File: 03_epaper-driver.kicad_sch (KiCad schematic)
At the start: 28 parts, among them J7 FFC2B28-24-G, Q1 Si1308EDL

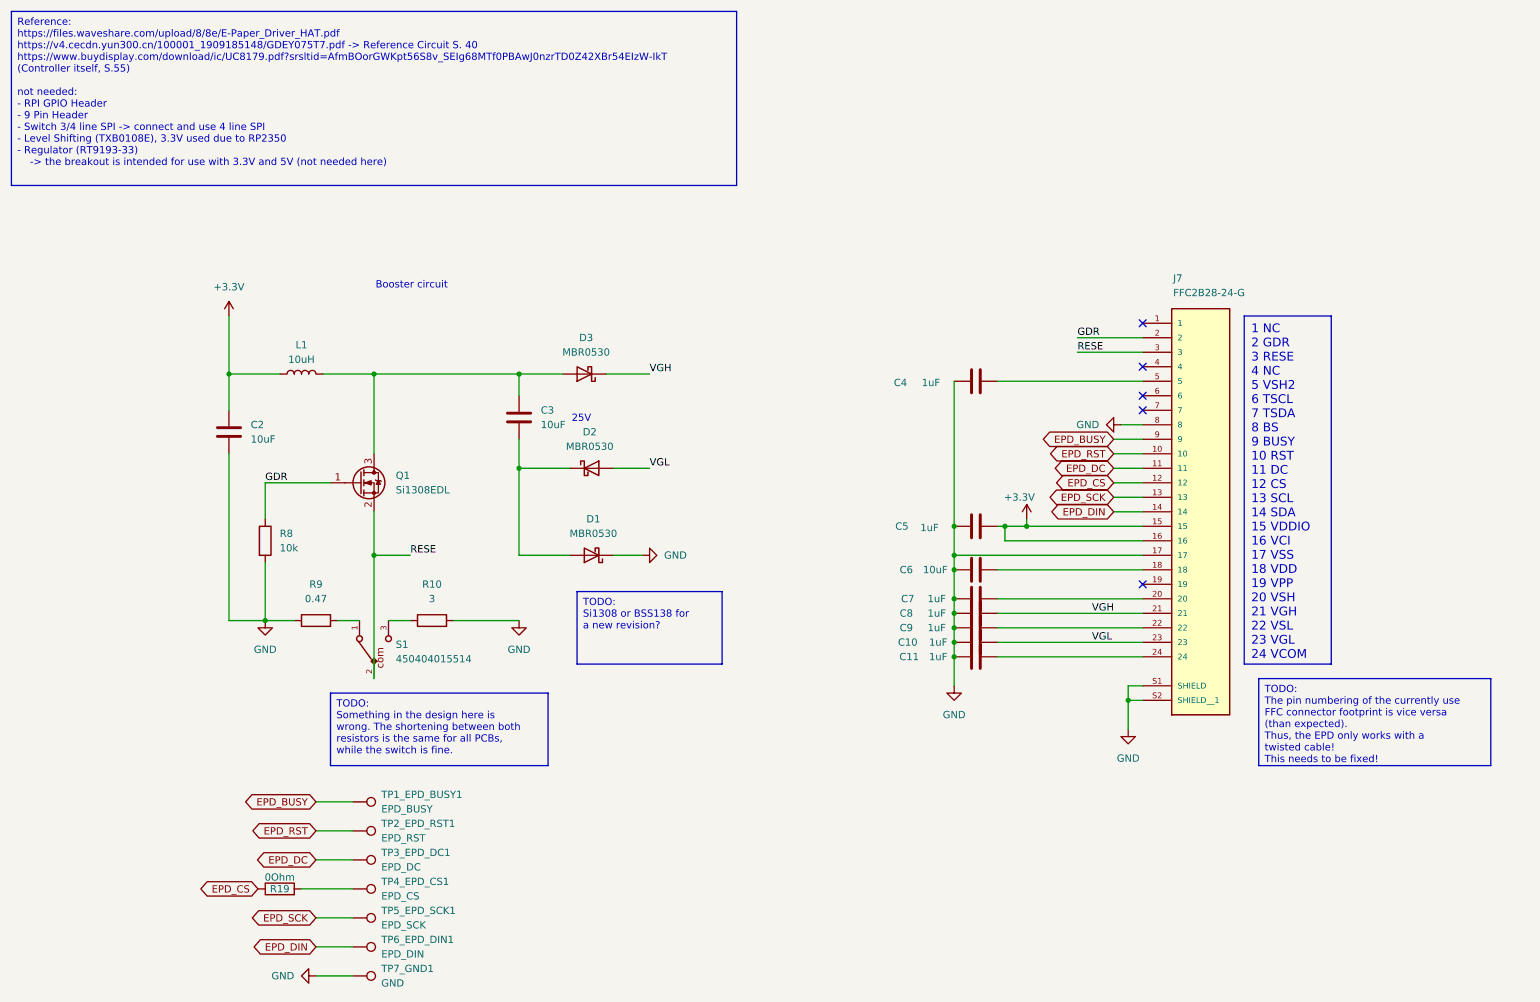
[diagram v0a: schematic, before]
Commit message: Migrate to KiCad 9, start working on the new revision
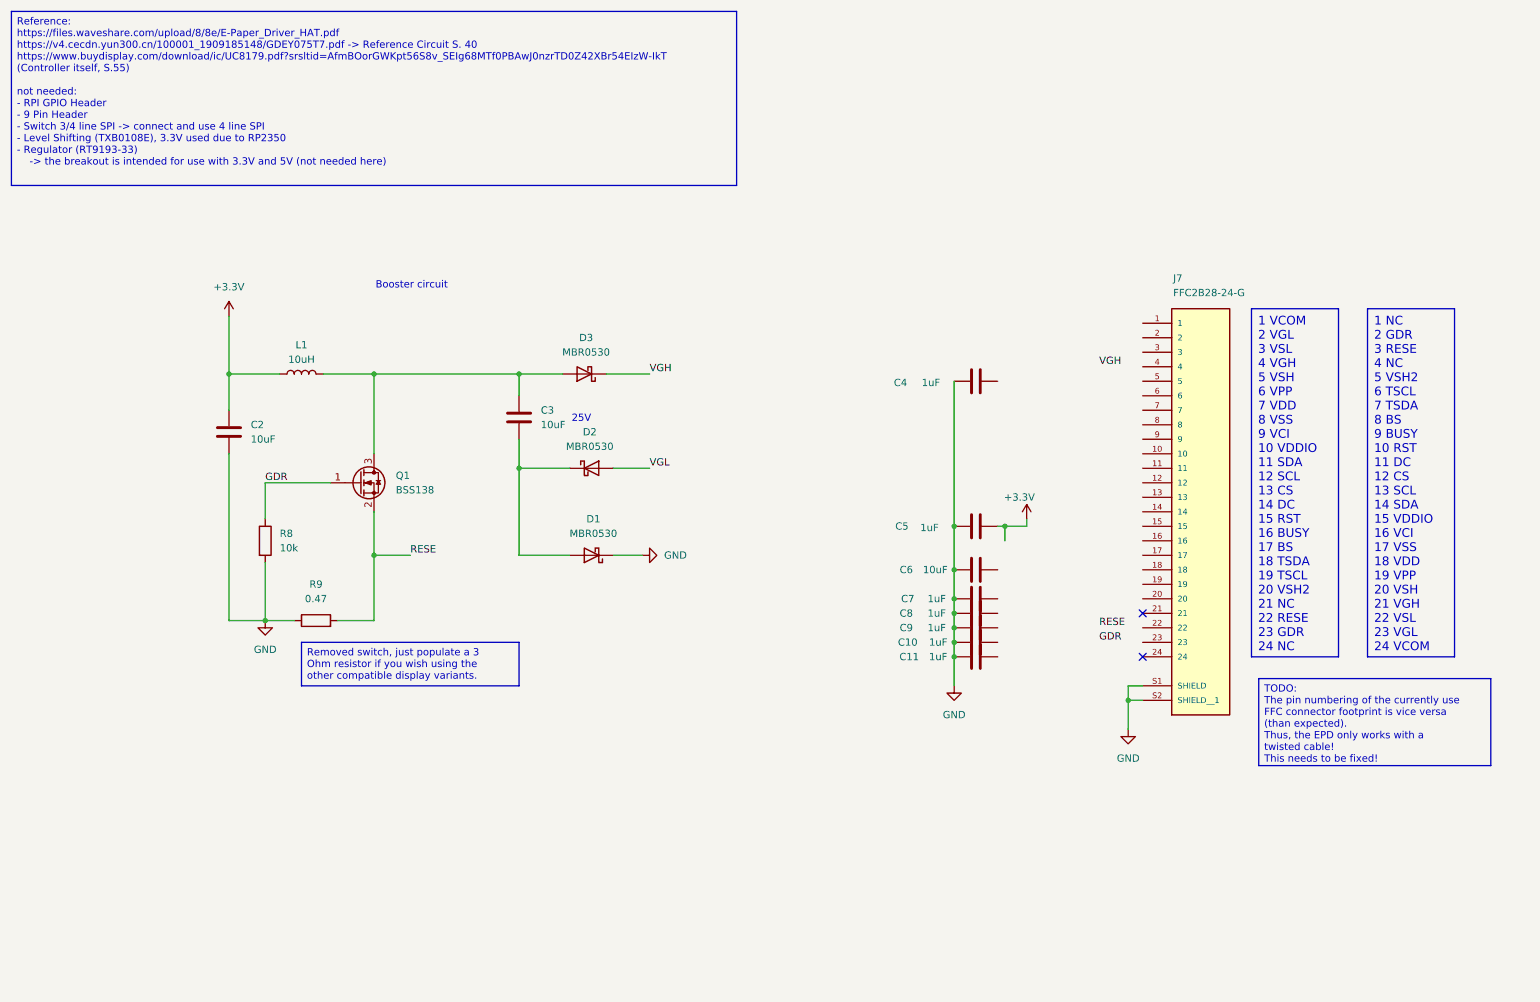
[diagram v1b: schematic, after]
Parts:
- removed Q1: Si1308EDL, Package_TO_SOT_SMD:SOT-323_SC-70, symbol Transistor_FET:Si1308EDL
- removed R10: 3, Resistor_SMD:R_1206_3216Metric_Pad1.30x1.75mm_HandSolder, symbol Device:R
- removed R19: 0Ohm, Resistor_SMD:R_1206_3216Metric_Pad1.30x1.75mm_HandSolder, symbol Device:R
- removed S1: 450404015514, prj-footprints:450404015514, symbol 450404015514:450404015514
- removed TP1_EPD_BUSY1: EPD_BUSY, TestPoint:TestPoint_Plated_Hole_D2.0mm, symbol Connector:TestPoint
- removed TP2_EPD_RST1: EPD_RST, TestPoint:TestPoint_Plated_Hole_D2.0mm, symbol Connector:TestPoint
- removed TP3_EPD_DC1: EPD_DC, TestPoint:TestPoint_Plated_Hole_D2.0mm, symbol Connector:TestPoint
- removed TP4_EPD_CS1: EPD_CS, TestPoint:TestPoint_Plated_Hole_D2.0mm, symbol Connector:TestPoint
- removed TP5_EPD_SCK1: EPD_SCK, TestPoint:TestPoint_Plated_Hole_D2.0mm, symbol Connector:TestPoint
- removed TP6_EPD_DIN1: EPD_DIN, TestPoint:TestPoint_Plated_Hole_D2.0mm, symbol Connector:TestPoint
- removed TP7_GND1: GND, TestPoint:TestPoint_Plated_Hole_D2.0mm, symbol Connector:TestPoint
- added Q1: BSS138, Package_TO_SOT_SMD:SOT-23, symbol Transistor_FET:BSS138
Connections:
- net +3.3V: no longer J7.15, J7.16
- net GDR: now also Q1.1 (G); no longer J7.2
- net GND: no longer J7.17, J7.8
- net RESE: now also R9.2, Q1.2 (S); no longer J7.3
- net VGH: no longer C8.2, J7.21
- net VGL: no longer C10.2, J7.23
- net at C3.1, D3.2 (A), L1.2: now also Q1.3 (D)
- net at C6.2: no longer J7.18
- net at J7.20: no longer C7.2
- net at J7.22: no longer C9.2
- net at J7.24: no longer C11.2
- net at J7.5: no longer C4.2
- net EPD_BUSY: no longer names the net of J7.9
- net EPD_CS: no longer names the net of J7.12
- net EPD_DC: no longer names the net of J7.11
- net EPD_DIN: no longer names the net of J7.14
- net EPD_RST: no longer names the net of J7.10
- net EPD_SCK: no longer names the net of J7.13
- no-connect marks 5 -> 2

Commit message: reworked epaper-driver schematic - corrected inverted ffc adapter
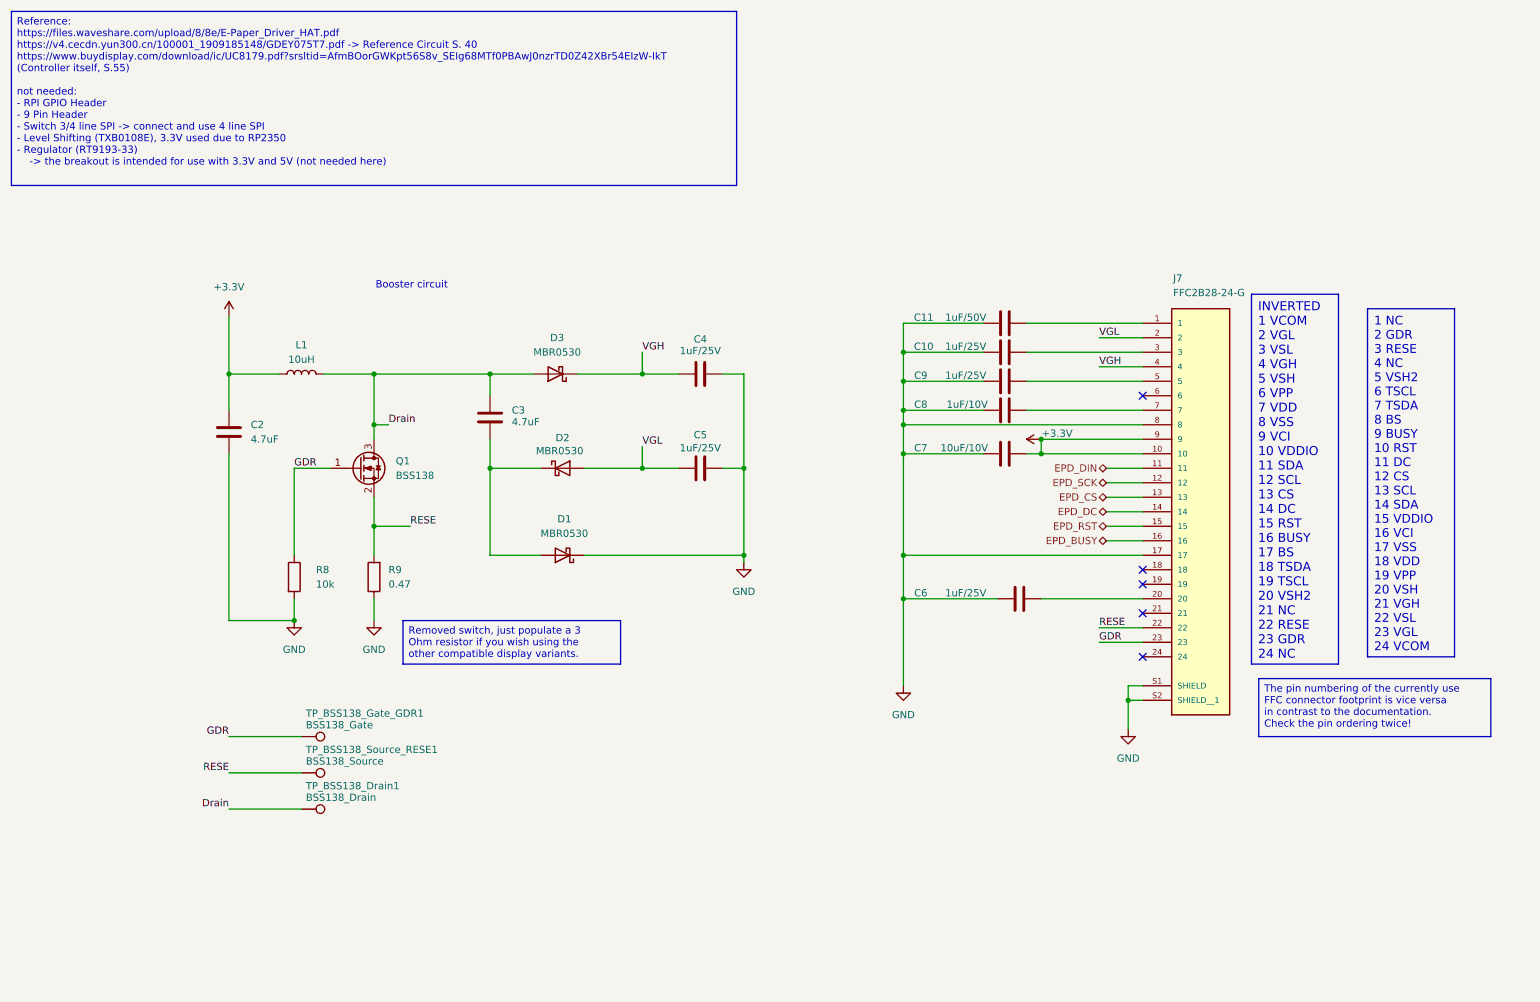
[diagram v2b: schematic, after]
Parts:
- added TP_BSS138_Drain1: BSS138_Drain, TestPoint:TestPoint_Pad_D2.5mm, symbol Connector:TestPoint
- added TP_BSS138_Gate_GDR1: BSS138_Gate, TestPoint:TestPoint_Pad_D2.5mm, symbol Connector:TestPoint
- added TP_BSS138_Source_RESE1: BSS138_Source, TestPoint:TestPoint_Pad_D2.5mm, symbol Connector:TestPoint
- C10: renamed from C8; value 1uF -> 1uF/25V
- C11: renamed from C10; value 1uF -> 1uF/50V
- C2, C3: value 10uF -> 4.7uF
- C4: renamed from C9; value 1uF -> 1uF/25V
- C5: renamed from C11; value 1uF -> 1uF/25V
- C6: renamed from C4; value 1uF -> 1uF/25V
- C7: renamed from C5; value 1uF -> 10uF/10V
- C8: renamed from C6; value 10uF -> 1uF/10V
- C9: renamed from C7; value 1uF -> 1uF/25V
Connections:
- net +3.3V: now also J7.10, J7.9
- net GDR: now also J7.23, TP_BSS138_Gate_GDR1.1
- net GND: now also C4.2, C5.2, J7.17, J7.8; no longer C4.1, C5.1
- net RESE: now also J7.22, TP_BSS138_Source_RESE1.1
- net VGH: now also C4.1, J7.4
- net VGL: now also C5.1, J7.2
- net at C10.2: now also J7.3
- net Drain: now reaches C3.1, D3.2 (A), L1.2, Q1.3 (D)
- net Drain: now also TP_BSS138_Drain1.1
- net at C8.2: now also J7.7
- net at J7.1: now also C11.2
- net EPD_DIN: now reaches J7.11
- net EPD_SCK: now reaches J7.12
- net EPD_CS: now reaches J7.13
- net EPD_DC: now reaches J7.14
- net EPD_RST: now reaches J7.15
- net EPD_BUSY: now reaches J7.16
- net at J7.20: now also C6.2
- net at J7.5: now also C9.2
- no-connect marks 2 -> 5
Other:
- note removed: "25V"
- moved on the sheet: C10, C11, C3, C4, C5, C6, C7, C8, C9, D1, D2, D3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

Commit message: switch to KiCad Pico extended symbol
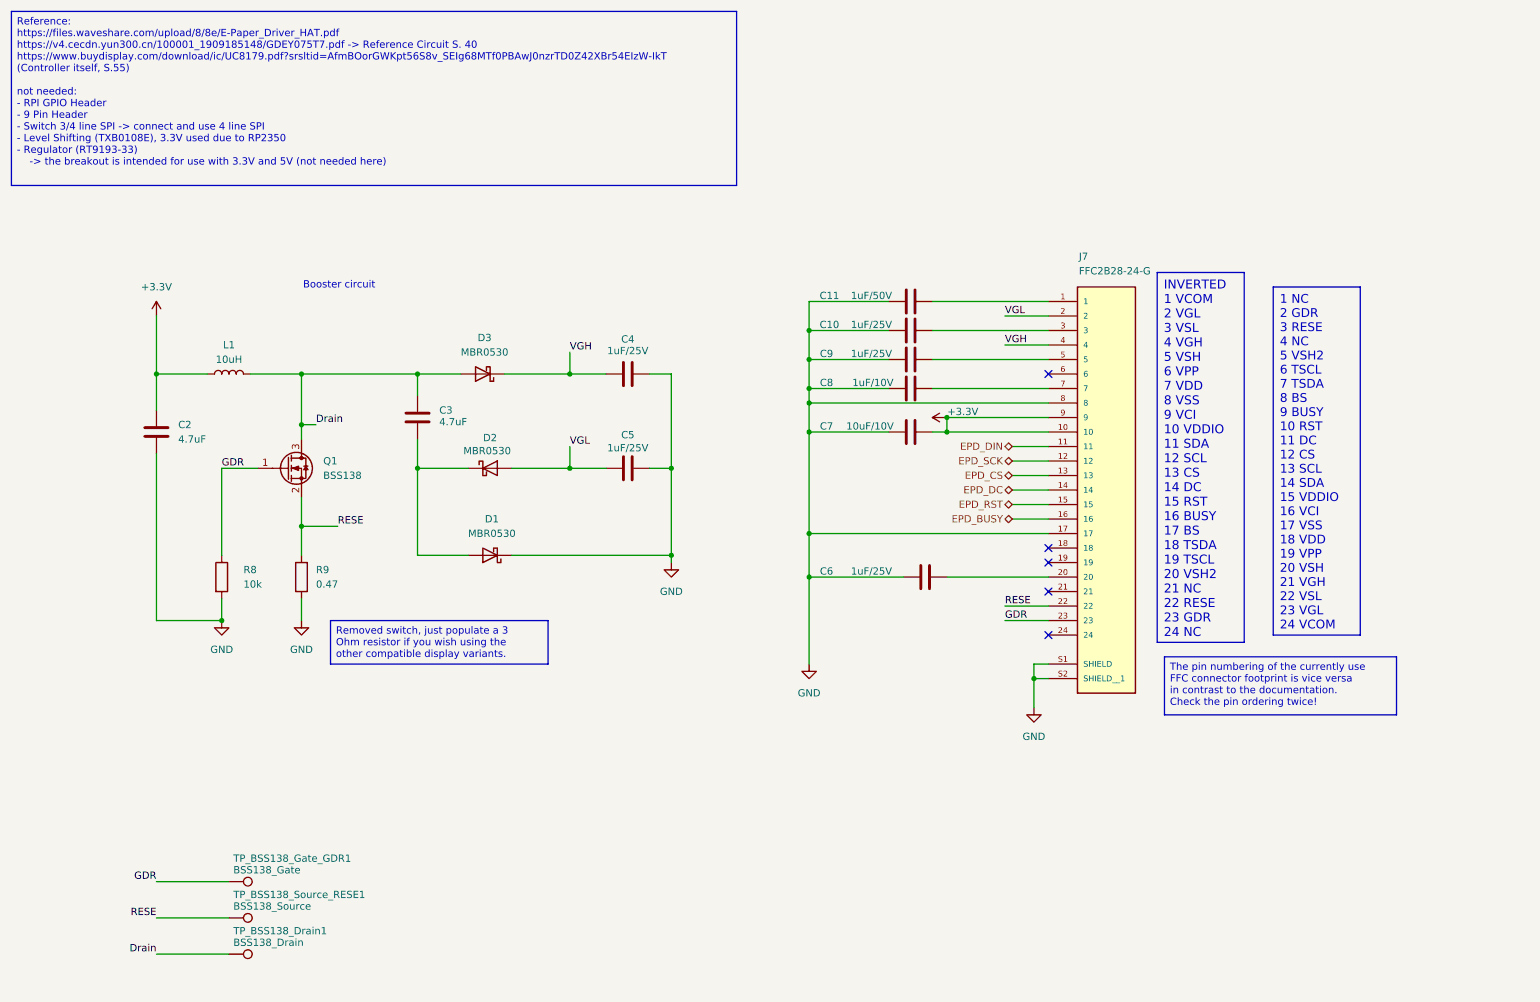
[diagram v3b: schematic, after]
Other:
- moved on the sheet: C10, C11, C2, C3, C4, C5, C6, C7, C8, C9, D1, D2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

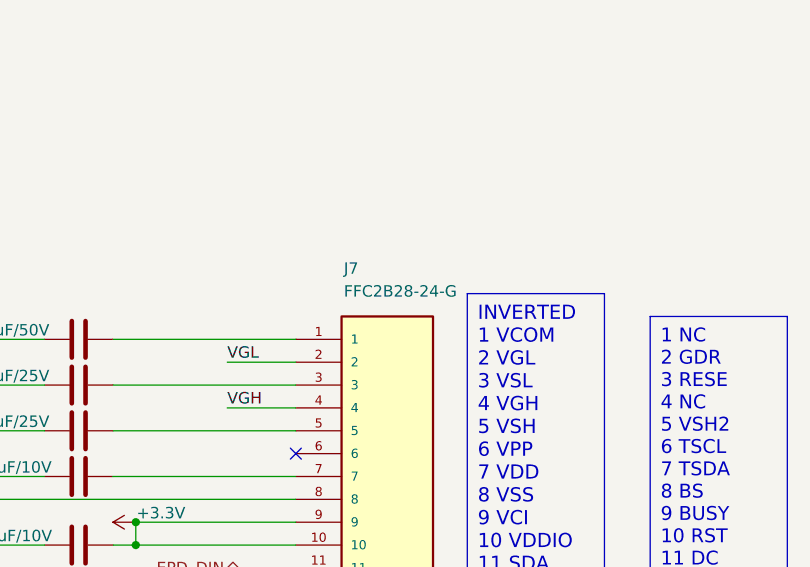
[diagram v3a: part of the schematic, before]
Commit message: fully connect the sd connector, redraw sd and buttons
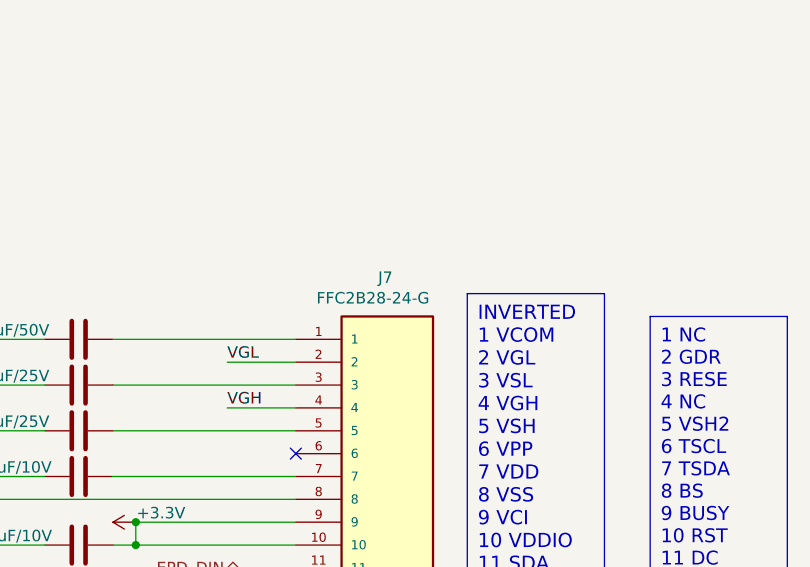
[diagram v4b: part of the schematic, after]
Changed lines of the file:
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@@
 		(dnp no)
 		(property "Reference" "J7"
-			(at 199.644 55.626 0)
+			(at 203.454 56.642 0)
 			(effects
 				(font
@@
 		)
 		(property "Value" "FFC2B28-24-G"
-			(at 199.644 58.166 0)
+			(at 196.596 58.928 0)
 			(effects
 				(font

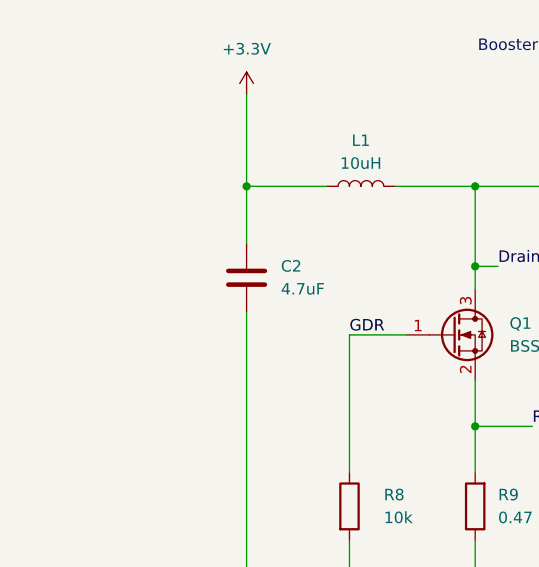
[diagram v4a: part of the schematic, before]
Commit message: updated power path, connect USB-C to pico's USB data
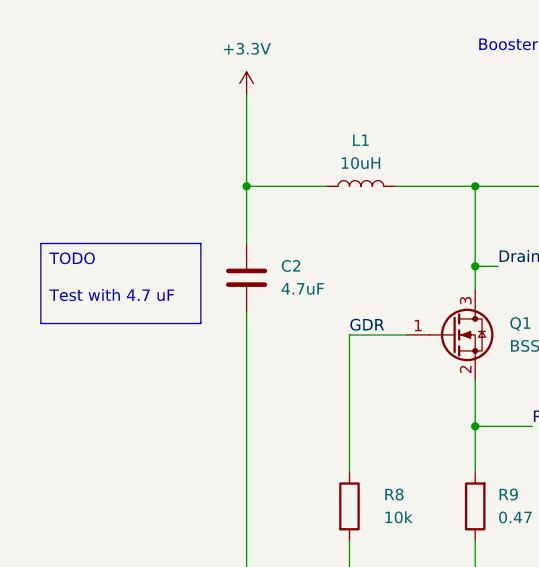
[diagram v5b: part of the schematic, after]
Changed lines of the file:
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@@
+		)
+	)
+	(text_box "TODO\n\nTest with 4.7 uF"
+		(exclude_from_sim no)
+		(at 15.24 82.55 0)
+		(size 17.78 8.89)
+		(margins 0.9525 0.9525 0.9525 0.9525)
+		(stroke
+			(width 0)
+			(type solid)
+		)
+		(fill
+			(type none)
+		)
+		(effects
+			(font
+				(size 1.27 1.27)
+			)
+			(justify left top)
 		)
 	)
